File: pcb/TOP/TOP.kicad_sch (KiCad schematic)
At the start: 91 parts

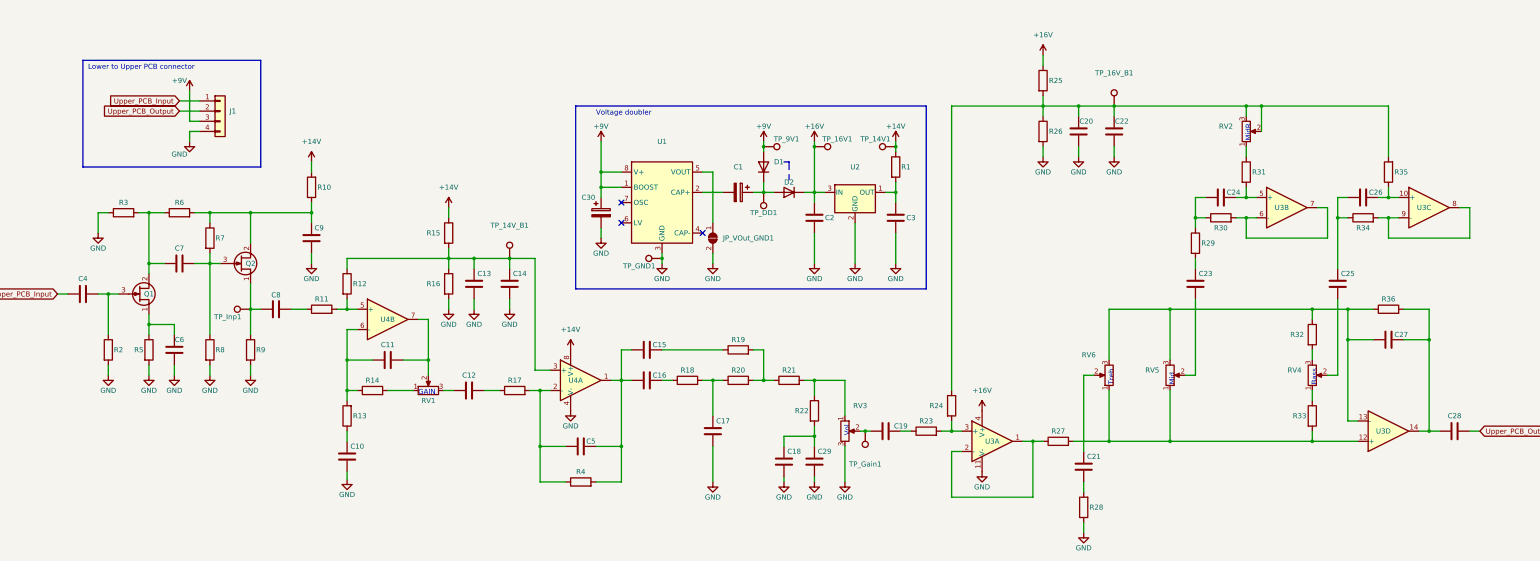
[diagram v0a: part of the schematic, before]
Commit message: [TOP] Route power, input and gain stages
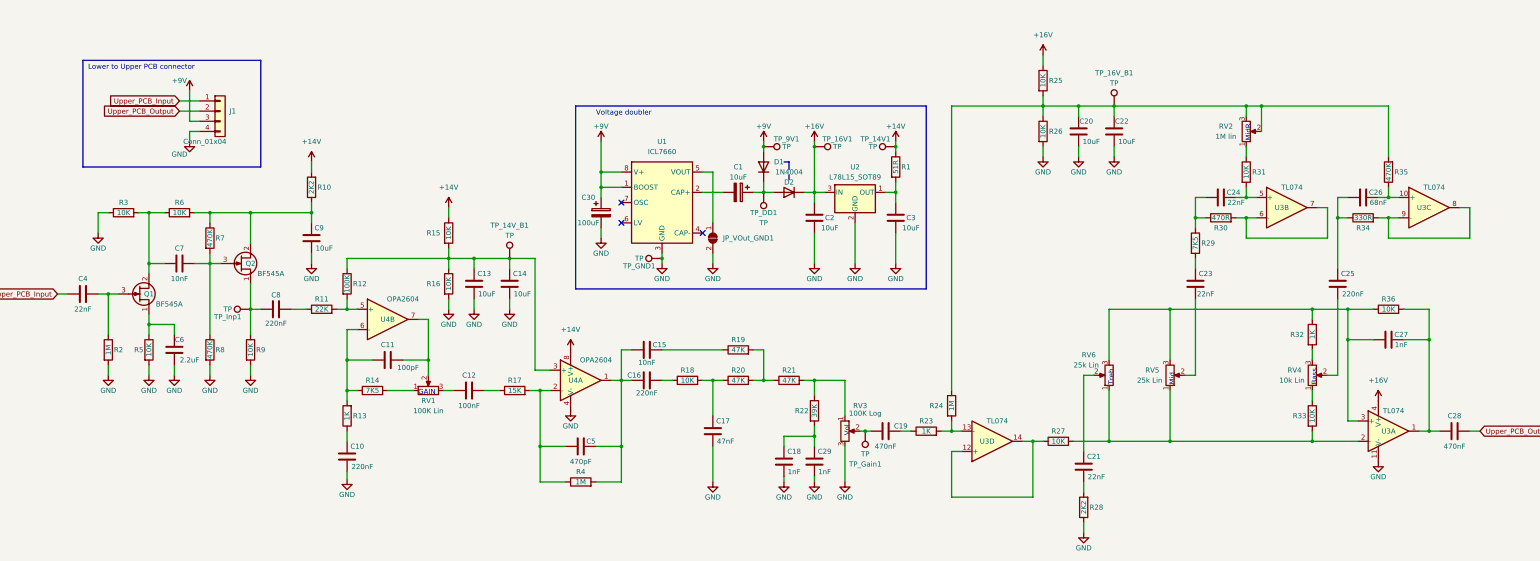
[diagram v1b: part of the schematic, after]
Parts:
- C1: value (none) -> 10uF; footprint (none) -> Capacitor_SMD:CP_Elec_4x5.4
- C10, C16, C25, C8: value (none) -> 220nF; footprint (none) -> Capacitor_SMD:C_0603_1608Metric
- C11: value (none) -> 100pF; footprint (none) -> Capacitor_SMD:C_0603_1608Metric
- C12: value (none) -> 100nF; footprint (none) -> Capacitor_SMD:C_0603_1608Metric
- C13, C14, C2, C20, C22, C3, C9: value (none) -> 10uF; footprint (none) -> Capacitor_SMD:C_0805_2012Metric
- C15, C7: value (none) -> 10nF; footprint (none) -> Capacitor_SMD:C_0805_2012Metric
- C17: value (none) -> 47nF; footprint (none) -> Capacitor_SMD:C_0603_1608Metric
- C18, C27, C29: value (none) -> 1nF; footprint (none) -> Capacitor_SMD:C_0603_1608Metric
- C19, C28: value (none) -> 470nF; footprint (none) -> Capacitor_SMD:C_0603_1608Metric
- C21, C23, C24, C4: value (none) -> 22nF; footprint (none) -> Capacitor_SMD:C_0603_1608Metric
- C26: value (none) -> 68nF; footprint (none) -> Capacitor_SMD:C_0603_1608Metric
- C30: value (none) -> 100uF; footprint (none) -> Capacitor_SMD:CP_Elec_6.3x5.4_Nichicon
- C5: value (none) -> 470pF; footprint (none) -> Capacitor_SMD:C_0603_1608Metric
- C6: value (none) -> 2.2uF; footprint (none) -> Capacitor_SMD:C_0603_1608Metric
- D1, D2: value (none) -> 1N4004; footprint (none) -> Diode_SMD:D_SMA
- J1: value (none) -> Conn_01x04; footprint (none) -> Connector_JST:JST_XH_B4B-XH-A_1x04_P2.50mm_Vertical
- JP_VOut_GND1: value (none) -> Jmp; footprint (none) -> Jumper:SolderJumper-2_P1.3mm_Open_TrianglePad1.0x1.5mm
- Q1, Q2: value (none) -> BF545A; footprint (none) -> Package_TO_SOT_SMD:SOT-23
- R1: value (none) -> 51R; footprint (none) -> Resistor_SMD:R_0603_1608Metric
- R10, R28: value (none) -> 2K2; footprint (none) -> Resistor_SMD:R_0603_1608Metric
- R11: value (none) -> 22K; footprint (none) -> Resistor_SMD:R_0603_1608Metric
- R12: value (none) -> 100K; footprint (none) -> Resistor_SMD:R_0603_1608Metric
- R13, R23, R32: value (none) -> 1K; footprint (none) -> Resistor_SMD:R_0603_1608Metric
- R14, R29: value (none) -> 7K5; footprint (none) -> Resistor_SMD:R_0603_1608Metric
- R15, R16, R18, R25, R26, R27, R3, R31, R33, R36, R5, R6, R9: value (none) -> 10K; footprint (none) -> Resistor_SMD:R_0603_1608Metric
- R17: value (none) -> 15K; footprint (none) -> Resistor_SMD:R_0603_1608Metric
- R19, R20, R21: value (none) -> 47K; footprint (none) -> Resistor_SMD:R_0603_1608Metric
- R2, R24, R4: value (none) -> 1M; footprint (none) -> Resistor_SMD:R_0603_1608Metric
- R22: value (none) -> 39K; footprint (none) -> Resistor_SMD:R_0603_1608Metric
- R30: value (none) -> 470R; footprint (none) -> Resistor_SMD:R_0603_1608Metric
- R34: value (none) -> 330R; footprint (none) -> Resistor_SMD:R_0603_1608Metric
- R35, R7, R8: value (none) -> 470K; footprint (none) -> Resistor_SMD:R_0603_1608Metric
- RV1: value (none) -> 100K Lin; footprint (none) -> MeineBib:Potentiometer_Alpha_RD901F-40-00D_Single_Vertical
- RV2: value (none) -> 1M lin; footprint (none) -> MeineBib:Potentiometer_Alpha_RD901F-40-00D_Single_Vertical
- RV3: value (none) -> 100K Log; footprint (none) -> MeineBib:Potentiometer_Alpha_RD901F-40-00D_Single_Vertical
- RV4: value (none) -> 10k Lin; footprint (none) -> MeineBib:Potentiometer_Alpha_RD901F-40-00D_Single_Vertical
- RV5, RV6: value (none) -> 25k Lin; footprint (none) -> MeineBib:Potentiometer_Alpha_RD901F-40-00D_Single_Vertical
- TP_14V1, TP_14V_B1, TP_16V1, TP_16V_B1, TP_9V1, TP_DD1, TP_GND1, TP_Gain1, TP_Inp1: value (none) -> TP; footprint (none) -> TestPoint:TestPoint_Pad_D2.0mm
- U1: value (none) -> ICL7660; footprint (none) -> Package_SO:SOP-8_3.9x4.9mm_P1.27mm
- U2: value (none) -> L78L15_SOT89; footprint (none) -> Package_TO_SOT_SMD:SOT-89-3
- U3: value (none) -> TL074; footprint (none) -> Package_SO:SOIC-14_3.9x8.7mm_P1.27mm
- U4: value (none) -> OPA2604; footprint (none) -> Package_SO:SOIC-8_3.9x4.9mm_P1.27mm
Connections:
- net at C15.2, C5.1, R4.2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: now also C16.1; no longer C16.2
- net at R27.2, R33.2, RV5.1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: now also U3.2 (-); no longer U3.12 (+)
- net at C27.2, R32.1, R36.1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: now also U3.3 (+); no longer U3.13 (-)
- net at R23.2, R24.2: now also U3.13 (-); no longer U3.3 (+)
- net at C27.1, C28.2, R36.2: now also U3.1; no longer U3.14
- net at R18.1: now also C16.2; no longer C16.1
- net +4V5 renamed +16V
- net +16V: no longer R1.1, R10.2, R15.1, TP_14V1.1, U4.8 (V+)
- new net: R27.1, U3.12 (+), U3.14
- new net +14V: R1.1, R10.2, R15.1, TP_14V1.1, U4.8 (V+)
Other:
- moved on the sheet: C16, U3A, U3D

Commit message: [TOP] Finish initial PCB design
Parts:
- removed TP_Gain1: TP, TestPoint:TestPoint_Pad_D2.0mm, symbol Connector:TestPoint
- Inp1: renamed from TP_Inp1; value TP -> (none); footprint TestPoint:TestPoint_Pad_D2.0mm -> (none)
- renumbered TP_14V1 to 14V1, TP_16V1 to 16V1, TP_9V1 to 9V1, TP_DD1 to DD1, TP_GND1 to GND1, JP_VOut_GND1 to VOut-GND1
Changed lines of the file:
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@@
   (junction (at 104.14 158.75) (diameter 0) (color 0 0 0 0)
   )
-  (junction (at 233.68 176.53) (diameter 0) (color 0 0 0 0)
-  )
   (junction (at 69.85 121.92) (diameter 0) (color 0 0 0 0)
   )
@@
     (stroke (width 0) (type default) (color 0 0 0 0))
   )
-  (wire (pts (xy 232.41 176.53) (xy 233.68 176.53))
+  (wire (pts (xy 232.41 176.53) (xy 234.95 176.53))
     (stroke (width 0) (type default) (color 0 0 0 0))
   )
@@
     (stroke (width 0) (type default) (color 0 0 0 0))
   )
-  (wire (pts (xy 233.68 176.53) (xy 234.95 176.53))
-    (stroke (width 0) (type default) (color 0 0 0 0))
-  )
   (wire (pts (xy 80.01 146.05) (xy 80.01 152.4))
     (stroke (width 0) (type default) (color 0 0 0 0))
@@
   (symbol (lib_id "Connector:TestPoint") (at 182.88 133.35 90) (unit 1)
     (in_bom no) (on_board yes)
-    (property "Reference" "TP_GND1" (id 0) (at 177.165 135.255 90))
+    (property "Reference" "GND1" (id 0) (at 177.165 135.255 90))
     (property "Value" "TP" (id 1) (at 177.165 133.35 90))
     (property "Footprint" "TestPoint:TestPoint_Pad_D2.0mm" (id 2) (at 182.88 128.27 0)
@@
   (symbol (lib_id "Connector:TestPoint") (at 241.3 105.41 90) (unit 1)
     (in_bom no) (on_board yes)
-    (property "Reference" "TP_14V1" (id 0) (at 236.22 103.505 90))
+    (property "Reference" "14V1" (id 0) (at 236.22 103.505 90))
     (property "Value" "TP" (id 1) (at 235.585 105.41 90))
     (property "Footprint" "TestPoint:TestPoint_Pad_D2.0mm" (id 2) (at 241.3 100.33 0)
@@
   (symbol (lib_id "Connector:TestPoint") (at 208.28 105.41 270) (unit 1)
     (in_bom no) (on_board yes)
-    (property "Reference" "TP_9V1" (id 0) (at 213.995 103.505 90))
+    (property "Reference" "9V1" (id 0) (at 213.995 103.505 90))
     (property "Value" "TP" (id 1) (at 213.995 105.41 90))
     (property "Footprint" "TestPoint:TestPoint_Pad_D2.0mm" (id 2) (at 208.28 110.49 0)
@@
   (symbol (lib_id "Connector:TestPoint") (at 80.01 146.05 90) (unit 1)
     (in_bom no) (on_board yes)
-    (property "Reference" "TP_Inp1" (id 0) (at 74.295 147.955 90))
-    (property "Value" "TP" (id 1) (at 74.295 146.05 90))
-    (property "Footprint" "TestPoint:TestPoint_Pad_D2.0mm" (id 2) (at 80.01 140.97 0)
+    (property "Reference" "Inp1" (id 0) (at 74.295 147.955 90))
+    (property "Value" "" (id 1) (at 74.295 146.05 90))
+    (property "Footprint" "" (id 2) (at 80.01 140.97 0)
       (effects (font (size 1.27 1.27)) hide)
     )
@@
   (symbol (lib_id "Jumper:SolderJumper_2_Open") (at 195.58 128.27 90) (mirror x) (unit 1)
     (in_bom no) (on_board yes)
-    (property "Reference" "JP_VOut_GND1" (id 0) (at 204.47 128.27 90))
+    (property "Reference" "VOut-GND1" (id 0) (at 203.2 128.27 90))
     (property "Value" "Jmp" (id 1) (at 200.66 128.27 0)
       (effects (font (size 1.27 1.27)) hide)
@@
   (symbol (lib_id "Connector:TestPoint") (at 220.98 105.41 270) (unit 1)
     (in_bom no) (on_board yes)
-    (property "Reference" "TP_16V1" (id 0) (at 226.695 103.505 90))
+    (property "Reference" "16V1" (id 0) (at 226.695 103.505 90))
     (property "Value" "TP" (id 1) (at 226.695 105.41 90))
     (property "Footprint" "TestPoint:TestPoint_Pad_D2.0mm" (id 2) (at 220.98 110.49 0)
@@
   (symbol (lib_id "Connector:TestPoint") (at 208.28 116.84 180) (unit 1)
     (in_bom no) (on_board yes)
-    (property "Reference" "TP_DD1" (id 0) (at 208.28 121.92 0))
+    (property "Reference" "DD1" (id 0) (at 208.28 121.92 0))
     (property "Value" "TP" (id 1) (at 208.28 124.46 0))
     (property "Footprint" "TestPoint:TestPoint_Pad_D2.0mm" (id 2) (at 203.2 116.84 0)
@@
     (pin "2")
   )
-  (symbol (lib_id "Connector:TestPoint") (at 233.68 176.53 180) (unit 1)
-    (in_bom no) (on_board yes)
-    (property "Reference" "TP_Gain1" (id 0) (at 233.68 184.785 0))
-    (property "Value" "TP" (id 1) (at 233.68 182.245 0))
-    (property "Footprint" "TestPoint:TestPoint_Pad_D2.0mm" (id 2) (at 228.6 176.53 0)
-      (effects (font (size 1.27 1.27)) hide)
-    )
-    (property "Datasheet" "~" (id 3) (at 228.6 176.53 0)
-      (effects (font (size 1.27 1.27)) hide)
-    )
-    (property "LCSC" "~" (id 4) (at 233.68 176.53 0)
-      (effects (font (size 1.27 1.27)) hide)
-    )
-    (pin "1")
-  )
   (symbol (lib_id "Device:C") (at 213.36 184.15 0) (unit 1)
     (in_bom yes) (on_board yes)
@@
       (reference "#PWR0125") (unit 1) (value "+9V") (footprint "")
     )
+    (path "/16343701-80cb-4ddd-be03-e72f0ff5bc43"
+      (reference "9V1") (unit 1) (value "TP") (footprint "TestPoint:TestPoint_Pad_D2.0mm")
+    )
+    (path "/15e53760-e6cc-4766-90d7-d2bd2dacdde4"
+      (reference "14V1") (unit 1) (value "TP") (footprint "TestPoint:TestPoint_Pad_D2.0mm")
+    )
+    (path "/bdab8a5b-8453-40e4-91f3-6b0116606b87"
+      (reference "16V1") (unit 1) (value "TP") (footprint "TestPoint:TestPoint_Pad_D2.0mm")
+    )
     (path "/33611798-ff99-4fbf-8304-671ca4cd15e2"
       (reference "C1") (unit 1) (value "10uF") (footprint "Capacitor_SMD:CP_Elec_4x5.4")
@@
       (reference "D2") (unit 1) (value "1N4004") (footprint "Diode_SMD:D_SMA")
     )
+    (path "/c20e6752-1d60-4673-993d-33ac47083931"
+      (reference "DD1") (unit 1) (value "TP") (footprint "TestPoint:TestPoint_Pad_D2.0mm")
+    )
+    (path "/10a748d1-06c5-4cb4-b4a0-a12855cde56a"
+      (reference "GND1") (unit 1) (value "TP") (footprint "TestPoint:TestPoint_Pad_D2.0mm")
+    )
+    (path "/3c238384-4bc3-4bea-a049-2a9f264ce82f"
+      (reference "Inp1") (unit 1) (value "TP") (footprint "TestPoint:TestPoint_Pad_D2.0mm")
+    )
     (path "/43624bd7-5b28-4455-bedf-a59e39f0128d"
       (reference "J1") (unit 1) (value "Conn_01x04") (footprint "Connector_JST:JST_XH_B4B-XH-A_1x04_P2.50mm_Vertical")
     )
-    (path "/3e425e3f-14fb-4fd6-bdf2-17f58f37086a"
-      (reference "JP_VOut_GND1") (unit 1) (value "Jmp") (footprint "Jumper:SolderJumper-2_P1.3mm_Open_TrianglePad1.0x1.5mm")
-    )
     (path "/b177607c-996f-4968-ab2d-792a31128235"
       (reference "Q1") (unit 1) (value "BF545A") (footprint "Package_TO_SOT_SMD:SOT-23")
@@
       (reference "RV6") (unit 1) (value "25k Lin") (footprint "MeineBib:Potentiometer_Alpha_RD901F-40-00D_Single_Vertical")
     )
-    (path "/16343701-80cb-4ddd-be03-e72f0ff5bc43"
-      (reference "TP_9V1") (unit 1) (value "TP") (footprint "TestPoint:TestPoint_Pad_D2.0mm")
-    )
-    (path "/15e53760-e6cc-4766-90d7-d2bd2dacdde4"
-      (reference "TP_14V1") (unit 1) (value "TP") (footprint "TestPoint:TestPoint_Pad_D2.0mm")
-    )
     (path "/37560992-9546-4c8f-93e1-57569b92ef2d"
       (reference "TP_14V_B1") (unit 1) (value "TP") (footprint "TestPoint:TestPoint_Pad_D2.0mm")
     )
-    (path "/bdab8a5b-8453-40e4-91f3-6b0116606b87"
-      (reference "TP_16V1") (unit 1) (value "TP") (footprint "TestPoint:TestPoint_Pad_D2.0mm")
-    )
     (path "/d6aac683-cd09-4e3e-b361-1c9a3df2bf43"
       (reference "TP_16V_B1") (unit 1) (value "TP") (footprint "TestPoint:TestPoint_Pad_D2.0mm")
     )
-    (path "/c20e6752-1d60-4673-993d-33ac47083931"
-      (reference "TP_DD1") (unit 1) (value "TP") (footprint "TestPoint:TestPoint_Pad_D2.0mm")
-    )
-    (path "/10a748d1-06c5-4cb4-b4a0-a12855cde56a"
-      (reference "TP_GND1") (unit 1) (value "TP") (footprint "TestPoint:TestPoint_Pad_D2.0mm")
-    )
-    (path "/d40396dd-d7af-4c1e-8689-7a4af0c4044d"
-      (reference "TP_Gain1") (unit 1) (value "TP") (footprint "TestPoint:TestPoint_Pad_D2.0mm")
-    )
-    (path "/3c238384-4bc3-4bea-a049-2a9f264ce82f"
-      (reference "TP_Inp1") (unit 1) (value "TP") (footprint "TestPoint:TestPoint_Pad_D2.0mm")
-    )
     (path "/b98d586a-f5ba-4430-8cee-d883948cc317"
       (reference "U1") (unit 1) (value "ICL7660") (footprint "Package_SO:SOP-8_3.9x4.9mm_P1.27mm")
@@
       (reference "U4") (unit 3) (value "OPA2604") (footprint "Package_SO:SOIC-8_3.9x4.9mm_P1.27mm")
     )
+    (path "/3e425e3f-14fb-4fd6-bdf2-17f58f37086a"
+      (reference "VOut-GND1") (unit 1) (value "Jmp") (footprint "Jumper:SolderJumper-2_P1.3mm_Open_TrianglePad1.0x1.5mm")
+    )
   )

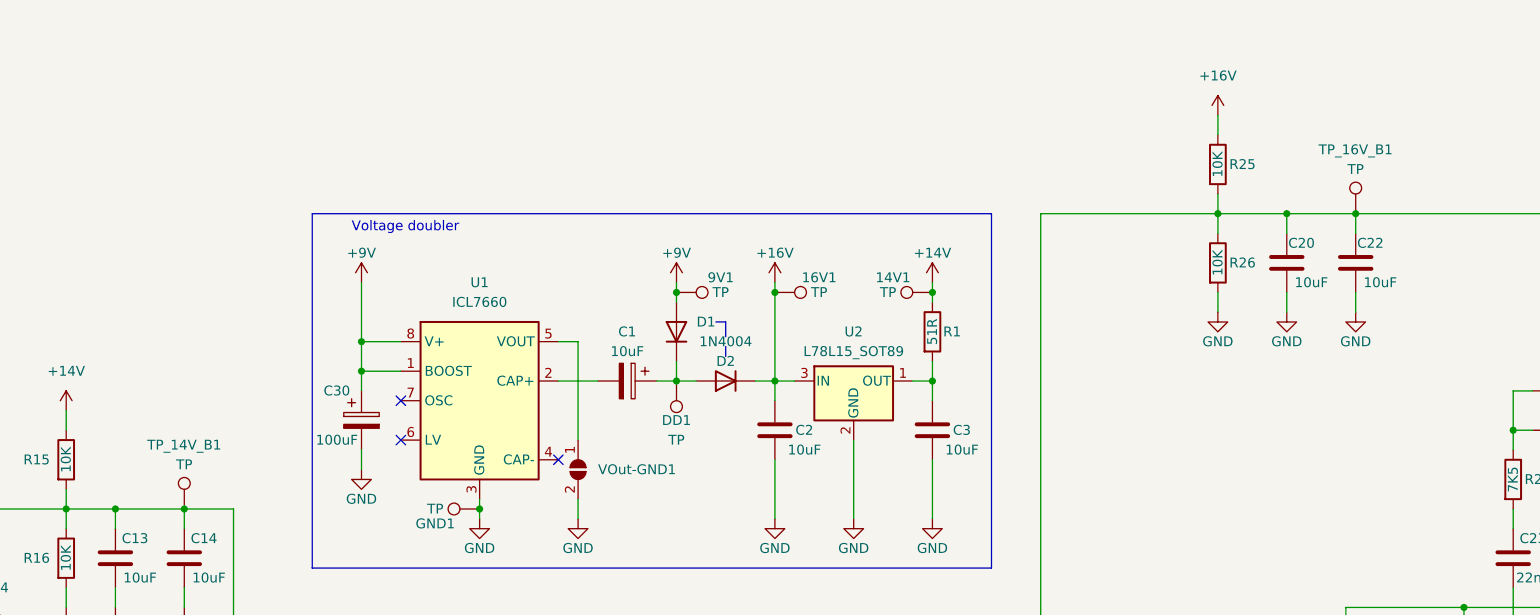
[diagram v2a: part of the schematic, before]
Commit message: [TOP] Forgot to save schematic after renaming testpoints
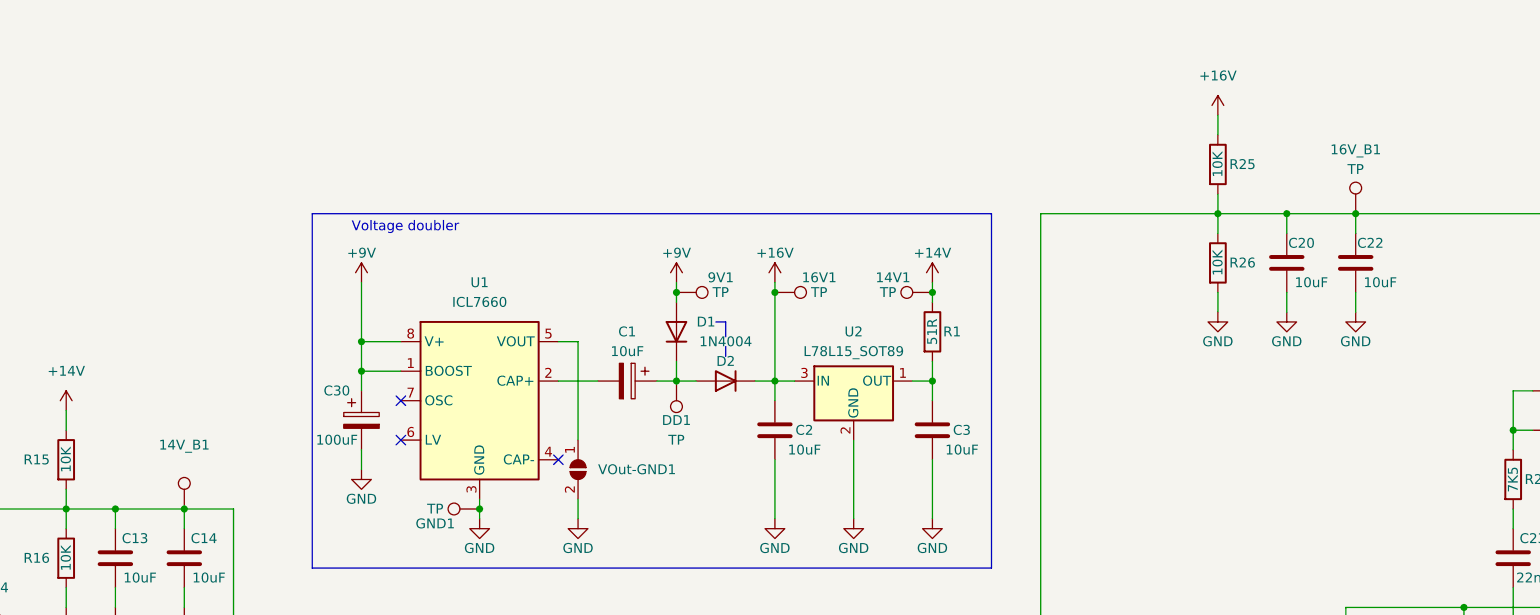
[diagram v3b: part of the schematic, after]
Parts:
- 14V_B1: renamed from TP_14V_B1; value TP -> (none); footprint TestPoint:TestPoint_Pad_D2.0mm -> (none)
- renumbered TP_16V_B1 to 16V_B1
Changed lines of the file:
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@@
   (symbol (lib_id "Connector:TestPoint") (at 144.78 133.35 0) (unit 1)
     (in_bom no) (on_board yes)
-    (property "Reference" "TP_14V_B1" (id 0) (at 144.78 125.095 0))
-    (property "Value" "TP" (id 1) (at 144.78 127.635 0))
-    (property "Footprint" "TestPoint:TestPoint_Pad_D2.0mm" (id 2) (at 149.86 133.35 0)
+    (property "Reference" "14V_B1" (id 0) (at 144.78 125.095 0))
+    (property "Value" "" (id 1) (at 144.78 127.635 0))
+    (property "Footprint" "" (id 2) (at 149.86 133.35 0)
       (effects (font (size 1.27 1.27)) hide)
     )
@@
   (symbol (lib_id "Connector:TestPoint") (at 295.91 95.25 0) (unit 1)
     (in_bom no) (on_board yes)
-    (property "Reference" "TP_16V_B1" (id 0) (at 295.91 86.995 0))
+    (property "Reference" "16V_B1" (id 0) (at 295.91 86.995 0))
     (property "Value" "TP" (id 1) (at 295.91 89.535 0))
     (property "Footprint" "TestPoint:TestPoint_Pad_D2.0mm" (id 2) (at 300.99 95.25 0)
@@
       (reference "14V1") (unit 1) (value "TP") (footprint "TestPoint:TestPoint_Pad_D2.0mm")
     )
+    (path "/37560992-9546-4c8f-93e1-57569b92ef2d"
+      (reference "14V_B1") (unit 1) (value "TP") (footprint "TestPoint:TestPoint_Pad_D2.0mm")
+    )
     (path "/bdab8a5b-8453-40e4-91f3-6b0116606b87"
       (reference "16V1") (unit 1) (value "TP") (footprint "TestPoint:TestPoint_Pad_D2.0mm")
     )
+    (path "/d6aac683-cd09-4e3e-b361-1c9a3df2bf43"
+      (reference "16V_B1") (unit 1) (value "TP") (footprint "TestPoint:TestPoint_Pad_D2.0mm")
+    )
     (path "/33611798-ff99-4fbf-8304-671ca4cd15e2"
       (reference "C1") (unit 1) (value "10uF") (footprint "Capacitor_SMD:CP_Elec_4x5.4")
@@
       (reference "RV6") (unit 1) (value "25k Lin") (footprint "MeineBib:Potentiometer_Alpha_RD901F-40-00D_Single_Vertical")
     )
-    (path "/37560992-9546-4c8f-93e1-57569b92ef2d"
-      (reference "TP_14V_B1") (unit 1) (value "TP") (footprint "TestPoint:TestPoint_Pad_D2.0mm")
-    )
-    (path "/d6aac683-cd09-4e3e-b361-1c9a3df2bf43"
-      (reference "TP_16V_B1") (unit 1) (value "TP") (footprint "TestPoint:TestPoint_Pad_D2.0mm")
-    )
     (path "/b98d586a-f5ba-4430-8cee-d883948cc317"
